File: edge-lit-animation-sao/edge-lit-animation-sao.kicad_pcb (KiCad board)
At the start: 2 copper layers, 60.3 x 50.8 mm, 70 parts, among them J1 USB_C_Receptacle_USB2.0_16P, J3 Conn_02x03_Odd_Even, SW1 SW_Push, SW2 SW_Push, SW3 SW_Push, SW4 SW_Push, U1 RP2040, U2 W25Q128JVS, U3 XC6206PxxxMR, U4 PAM8301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

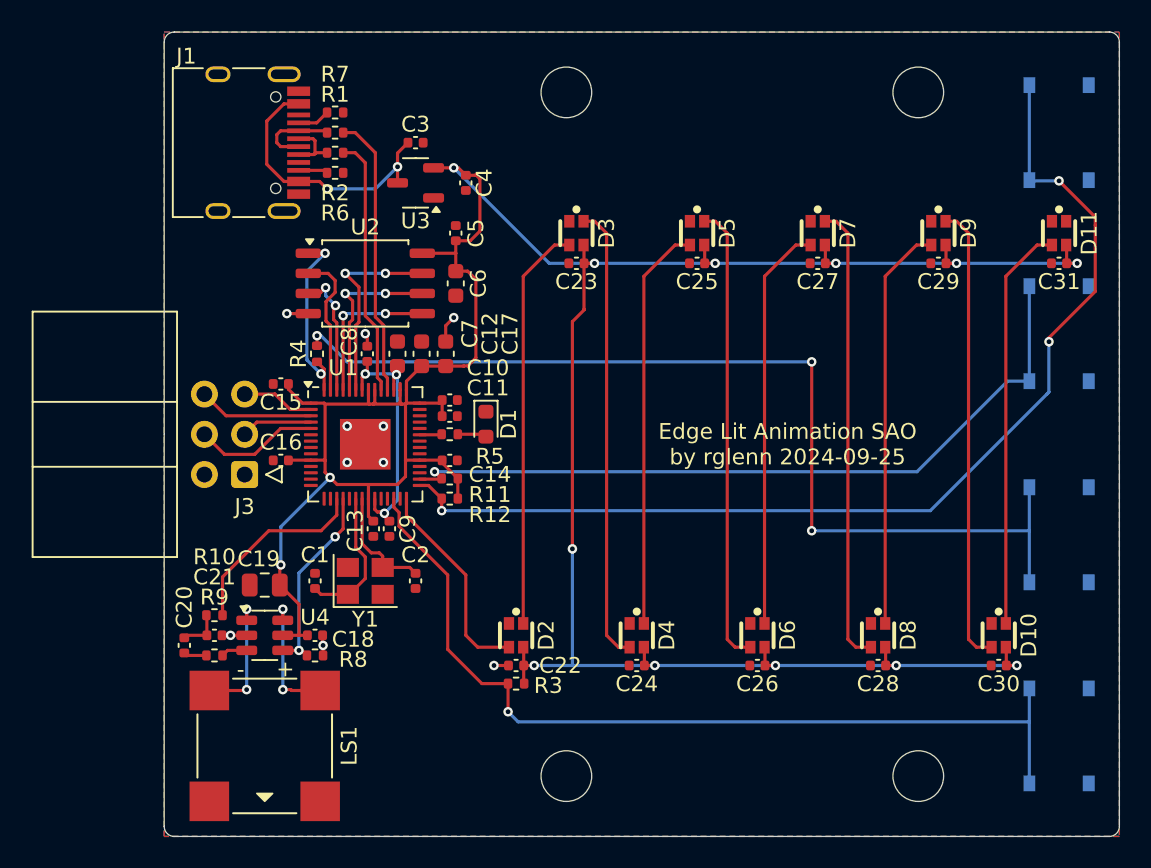
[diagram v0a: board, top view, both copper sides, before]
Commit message: Changing from WS2812s to standard white LEDs
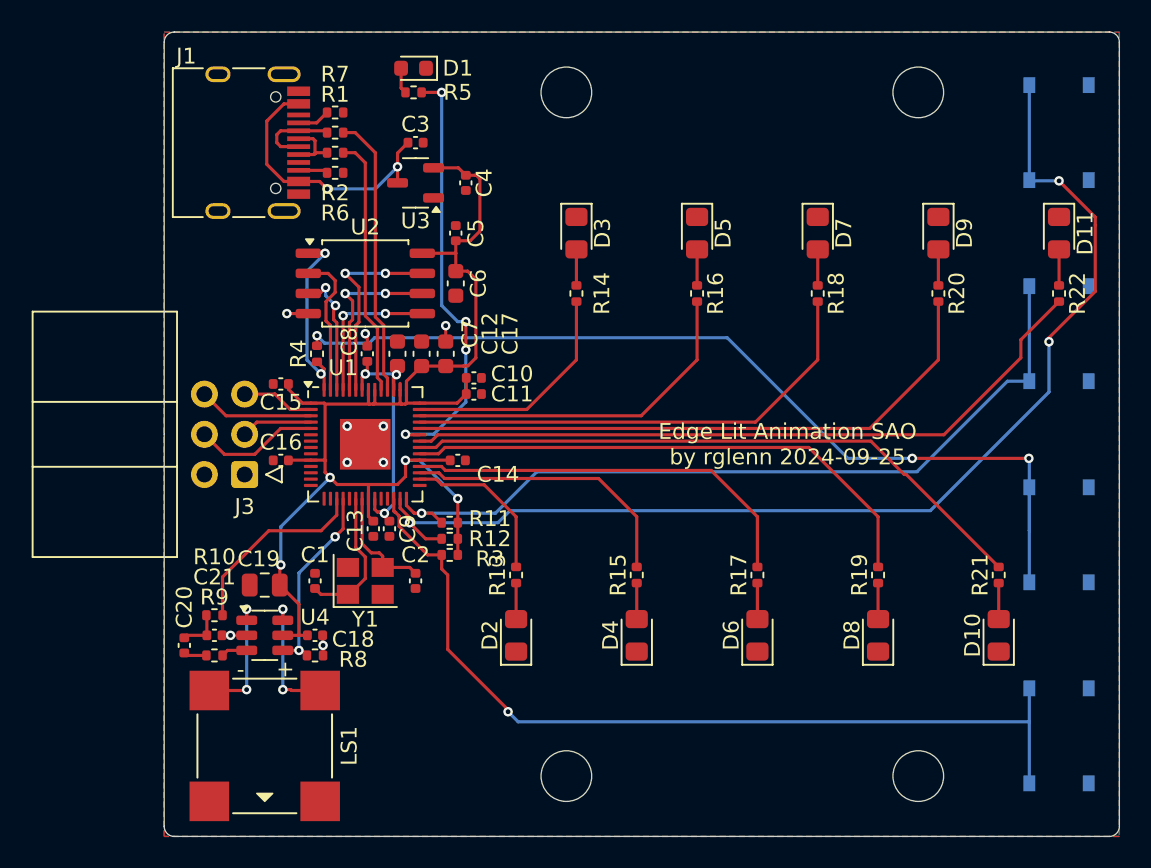
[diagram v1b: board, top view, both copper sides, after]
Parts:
- removed C22, C23, C24, C25, C26, C27, C28, C29, C30, C31: 1u, Capacitor_SMD:C_0402_1005Metric
- added R13: 470, Resistor_SMD:R_0402_1005Metric, F.Cu at (136.5, 110.5)
- added R14: 470, Resistor_SMD:R_0402_1005Metric, F.Cu at (140.3, 92.7)
- added R15: 470, Resistor_SMD:R_0402_1005Metric, F.Cu at (144.1, 110.5)
- added R16: 470, Resistor_SMD:R_0402_1005Metric, F.Cu at (148.0, 92.7)
- added R17: 470, Resistor_SMD:R_0402_1005Metric, F.Cu at (151.8, 110.5)
- added R18: 470, Resistor_SMD:R_0402_1005Metric, F.Cu at (155.6, 92.7)
- added R19: 470, Resistor_SMD:R_0402_1005Metric, F.Cu at (159.4, 110.5)
- added R20: 470, Resistor_SMD:R_0402_1005Metric, F.Cu at (163.2, 92.7)
- added R21: 470, Resistor_SMD:R_0402_1005Metric, F.Cu at (167.0, 110.5)
- added R22: 470, Resistor_SMD:R_0402_1005Metric, F.Cu at (170.8, 92.7)
- D10, D11, D2, D3, D4, D5, D6, D7, D8, D9: value XL-1615RGBC-WS2812B -> LED; footprint edge-lit-parts:LED-SMD_4P-L1.6-W1.5_XL-1615RGBC-WS2812B -> LED_SMD:LED_0805_2012Metric_Pad1.15x1.40mm_HandSolder
- moved D1 22.9 mm to (130.0, 78.5), turned to 180 degrees
- moved R5 21.7 mm to (130.0, 80.0), turned to 0 degrees
- moved R3 9.14 mm to (132.3, 109.2)
- moved R11 2.79 mm to (132.3, 107.2)
- moved R12 2.54 mm to (132.3, 108.2)
- moved C10 2.07 mm to (133.9, 98.0)
- moved C11 2.07 mm to (133.9, 99.1)
- moved C14 0.51 mm to (132.8, 103.3)
- turned D10 to 90 degrees
- turned D2 to 90 degrees
- turned D4 to 90 degrees
- turned D6 to 90 degrees
- turned D8 to 90 degrees
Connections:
- D10 pad 1: Net-(D10-DOUT) -> GND
- D10 pad 2: +3V3 -> Net-(D10-A)
- D11 pad 1: unconnected-(D11-DOUT-Pad1) -> GND
- D11 pad 2: +3V3 -> Net-(D11-A)
- D2 pad 1: Net-(D2-DOUT) -> GND
- D2 pad 2: +3V3 -> Net-(D2-A)
- D3 pad 1: Net-(D3-DOUT) -> GND
- D3 pad 2: +3V3 -> Net-(D3-A)
- D4 pad 1: Net-(D4-DOUT) -> GND
- D4 pad 2: +3V3 -> Net-(D4-A)
- D5 pad 1: Net-(D5-DOUT) -> GND
- D5 pad 2: +3V3 -> Net-(D5-A)
- D6 pad 1: Net-(D6-DOUT) -> GND
- D6 pad 2: +3V3 -> Net-(D6-A)
- D7 pad 1: Net-(D7-DOUT) -> GND
- D7 pad 2: +3V3 -> Net-(D7-A)
- D8 pad 1: Net-(D8-DOUT) -> GND
- D8 pad 2: +3V3 -> Net-(D8-A)
- D9 pad 1: Net-(D10-DIN) -> GND
- D9 pad 2: +3V3 -> Net-(D9-A)
- U1 pad 27: unconnected-(U1-GPIO16-Pad27) -> /BUTTON2
- U1 pad 28: Net-(D2-DIN) -> /BUTTON1
- U1 pad 29: /BUTTON2 -> unconnected-(U1-GPIO18-Pad29)
- U1 pad 30: /BUTTON1 -> Net-(U1-GPIO19)
- U1 pad 31: unconnected-(U1-GPIO20-Pad31) -> Net-(U1-GPIO20)
- U1 pad 32: unconnected-(U1-GPIO21-Pad32) -> Net-(U1-GPIO21)
- U1 pad 34: unconnected-(U1-GPIO22-Pad34) -> Net-(U1-GPIO22)
- U1 pad 35: unconnected-(U1-GPIO23-Pad35) -> Net-(U1-GPIO23)
- U1 pad 36: unconnected-(U1-GPIO24-Pad36) -> Net-(U1-GPIO24)
- U1 pad 38: unconnected-(U1-GPIO26_ADC0-Pad38) -> Net-(U1-GPIO26_ADC0)
- U1 pad 39: unconnected-(U1-GPIO27_ADC1-Pad39) -> Net-(U1-GPIO27_ADC1)
- U1 pad 40: unconnected-(U1-GPIO28_ADC2-Pad40) -> Net-(U1-GPIO28_ADC2)
- U1 pad 41: unconnected-(U1-GPIO29_ADC3-Pad41) -> Net-(U1-GPIO29_ADC3)
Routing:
- net +3V3: track 195.2 -> 81.6 mm, vias 14 -> 4
- net Net-(U1-GPIO24): track 0.00 -> 44.7 mm
- net Net-(U1-GPIO23): track 0.00 -> 40.0 mm
- net Net-(U1-GPIO26_ADC0): track 0.00 -> 38.2 mm
- net Net-(U1-GPIO22): track 0.00 -> 34.1 mm
- net Net-(U1-GPIO27_ADC1): track 0.00 -> 30.4 mm
- net Net-(D5-DOUT): track 29.1 -> 0.00 mm
- net Net-(D7-DOUT): track 29.1 -> 0.00 mm
- net Net-(D10-DIN): track 29.1 -> 0.00 mm
- net Net-(D3-DOUT): track 28.9 -> 0.00 mm
- net /LED: track 1.40 -> 27.3 mm, vias 0 -> 4
- net Net-(U1-GPIO21): track 0.00 -> 25.8 mm
- net Net-(D8-DOUT): track 25.7 -> 0.00 mm
- net Net-(D6-DOUT): track 25.7 -> 0.00 mm
- net Net-(D4-DOUT): track 25.7 -> 0.00 mm
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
